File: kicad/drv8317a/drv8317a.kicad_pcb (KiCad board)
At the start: 2 copper layers, 15 parts, among them J1 Conn_01x08_Pin, J2 Conn_01x02_Pin, J3 Conn_01x03_Pin, J4 Conn_01x06_Pin, U1 DRV8317H

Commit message: 100% routed, review needed
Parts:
- NT1: moved to B.Cu
- moved J1 83.9 mm to (170.1, 110.4), turned to -90 degrees
- moved R1 68.8 mm to (163.3, 114.4), turned to -90 degrees
- moved J4 65.0 mm to (152.4, 126.7), turned to 180 degrees
- moved C4 8.45 mm to (164.7, 127.0)
- moved J2 8.19 mm to (178.8, 133.0), turned to 180 degrees
- moved C3 7.96 mm to (164.5, 128.8)
- moved C8 6.65 mm to (166.2, 124.3)
- moved NT1 6.04 mm to (168.8, 130.7)
- moved C9 1.75 mm to (163.3, 117.7), turned to 90 degrees
- moved C6 1.50 mm to (168.3, 126.1)
- moved C5 1.49 mm to (169.6, 114.3), turned to 0 degrees
- moved C7 1.30 mm to (169.8, 124.3)
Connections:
- J1 pad 1: /nSLEEP -> /INHA
- J1 pad 2: /INHA -> /INHB
- J1 pad 3: /INHB -> /INHC
- J1 pad 4: /INHC -> /INL
- J1 pad 5: /INL -> /GAIN
- J1 pad 6: /GAIN -> /SLEW
- J1 pad 7: /SLEW -> /MODE
- J1 pad 8: /MODE -> /nSLEEP
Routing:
- net GNDA: track 2.07 -> 30.6 mm, vias 0 -> 2
- net /INL: track 0.00 -> 24.9 mm, vias 0 -> 2
- net /nSLEEP: track 0.00 -> 22.4 mm, vias 0 -> 2
- net /nFAULT: track 0.00 -> 17.0 mm
- net /MODE: track 0.00 -> 15.2 mm
- net /SOA: track 0.00 -> 14.8 mm
- net /SLEW: track 0.00 -> 13.9 mm
- net /SOB: track 0.00 -> 13.9 mm
- net GNDPWR: track 7.90 -> 21.4 mm, vias 4 -> 11
- net /SOC: track 0.00 -> 13.4 mm
- net VDDA: track 0.00 -> 11.5 mm, vias 0 -> 2
- net /GAIN: track 0.00 -> 11.0 mm
- net +BATT: track 11.6 -> 21.5 mm, vias 2 -> 7
- net /INHA: track 0.00 -> 8.07 mm
- net /INHB: track 0.00 -> 7.43 mm
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- added copper zone on B.Cu, net +BATT
- added copper zone on B.Cu, net GNDA
- added copper zone on B.Cu, net GNDPWR
- added copper zone on F.Cu, net GNDPWR
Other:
- board outline added: 31.3 x 25.2 mm

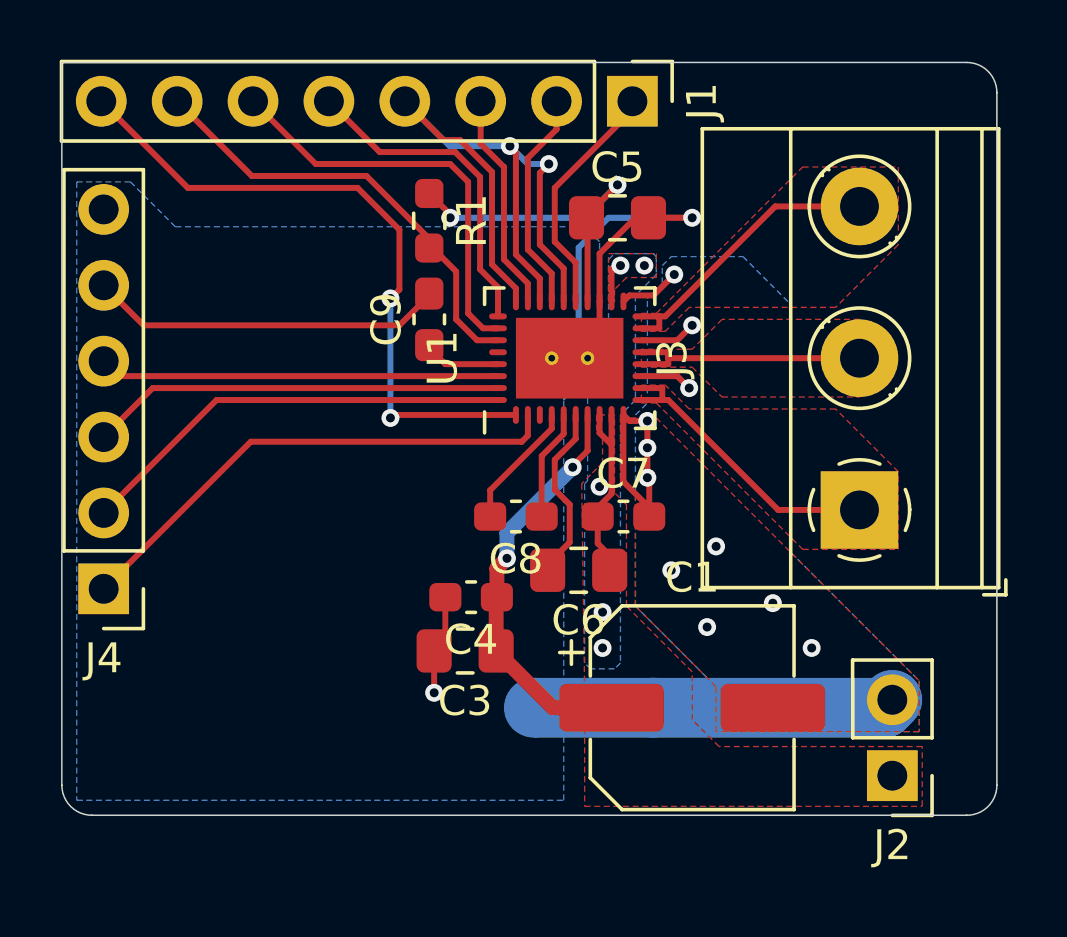
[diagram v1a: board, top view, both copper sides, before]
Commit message: config: use resistors instead of mcu signals
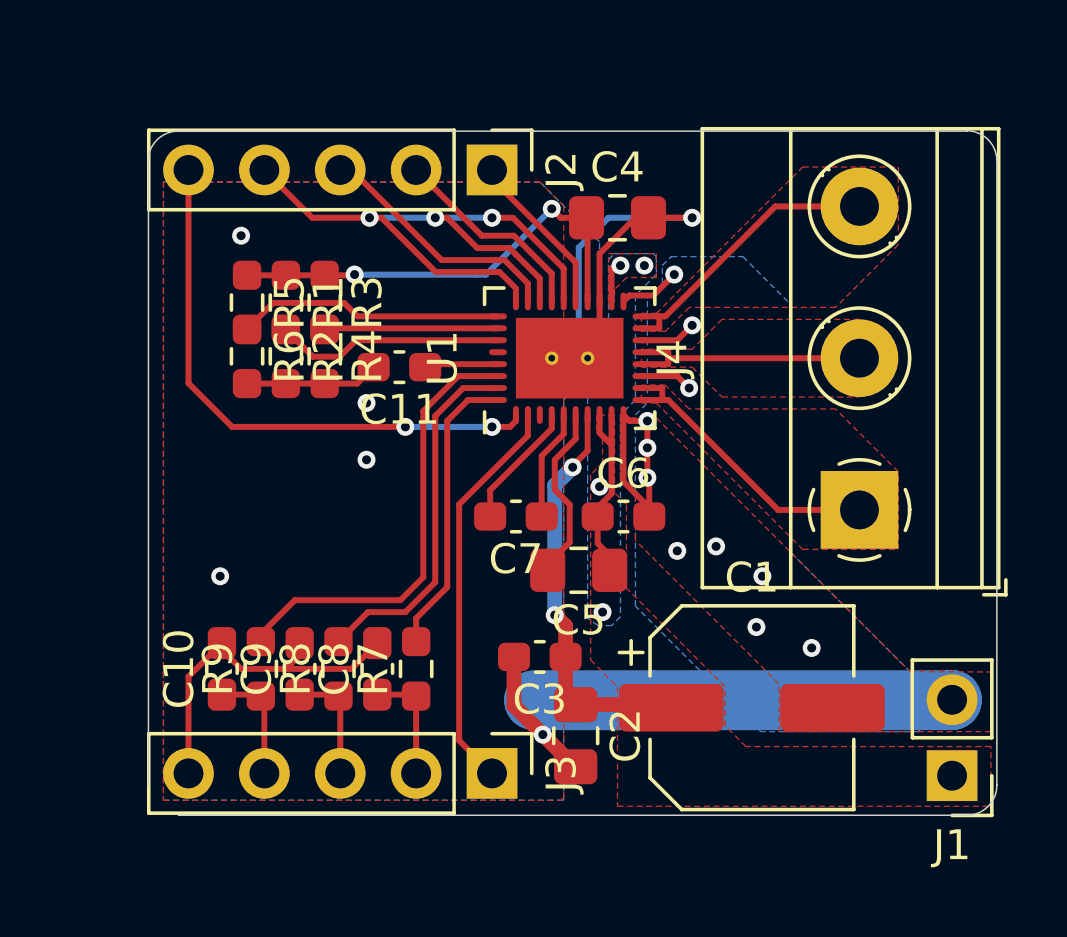
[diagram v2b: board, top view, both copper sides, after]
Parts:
- removed the J1 at (170.1, 110.4)
- removed the J4 at (152.4, 126.7)
- added C10: 22pF, Capacitor_SMD:C_0603_1608Metric_Pad1.08x0.95mm_HandSolder, F.Cu at (156.4, 129.4)
- added C8: 22pF, Capacitor_SMD:C_0603_1608Metric_Pad1.08x0.95mm_HandSolder, F.Cu at (161.6, 129.4)
- added C9: 22pF, Capacitor_SMD:C_0603_1608Metric_Pad1.08x0.95mm_HandSolder, F.Cu at (159.0, 129.4)
- added J2: Conn_01x05_Pin, Connector_PinHeader_2.54mm:PinHeader_1x05_P2.54mm_Vertical, F.Cu at (165.4, 112.7)
- added J3: Conn_01x05_Pin, Connector_PinHeader_2.54mm:PinHeader_1x05_P2.54mm_Vertical, F.Cu at (165.4, 132.9)
- added R2: NC, Resistor_SMD:R_0603_1608Metric_Pad0.98x0.95mm_HandSolder, F.Cu at (158.5, 118.9)
- added R3: NC, Resistor_SMD:R_0603_1608Metric_Pad0.98x0.95mm_HandSolder, F.Cu at (159.8, 117.1)
- added R4: NC, Resistor_SMD:R_0603_1608Metric_Pad0.98x0.95mm_HandSolder, F.Cu at (159.8, 118.9)
- added R5: NC, Resistor_SMD:R_0603_1608Metric_Pad0.98x0.95mm_HandSolder, F.Cu at (157.2, 117.1)
- added R6: NC, Resistor_SMD:R_0603_1608Metric_Pad0.98x0.95mm_HandSolder, F.Cu at (157.2, 118.9)
- added R7: 330R, Resistor_SMD:R_0603_1608Metric_Pad0.98x0.95mm_HandSolder, F.Cu at (162.9, 129.4)
- added R8: 330R, Resistor_SMD:R_0603_1608Metric_Pad0.98x0.95mm_HandSolder, F.Cu at (160.3, 129.4)
- added R9: 330R, Resistor_SMD:R_0603_1608Metric_Pad0.98x0.95mm_HandSolder, F.Cu at (157.7, 129.4)
- R1: value 10k -> NC
- moved R1 5.53 mm to (158.5, 117.1)
- moved C2 4.66 mm to (168.2, 131.6), turned to -90 degrees
- moved C3 3.05 mm to (167.0, 129.0)
- moved C1 2.00 mm to (174.1, 130.7)
- moved J1 2.00 mm to (180.8, 133.0)
- moved C11 1.89 mm to (162.3, 119.3), turned to 180 degrees
- moved NT1 0.25 mm to (168.8, 130.4)
- renumbered C9 to C11, C3 to C2, C4 to C3, C5 to C4, C6 to C5, C7 to C6, C8 to C7, J2 to J1, J3 to J4
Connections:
- net Net-(U1-CSA_REF) renamed /CSA
- U1 pad 34: /SOC -> Net-(U1-SOC)
- U1 pad 35: /SOB -> Net-(U1-SOB)
- U1 pad 36: /SOA -> Net-(U1-SOA)
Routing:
- net Net-(U1-SOC): track 0.00 -> 15.0 mm
- net Net-(U1-SOB): track 0.00 -> 12.4 mm
- net /SOA: track 14.8 -> 3.91 mm
- net /SOB: track 13.9 -> 3.93 mm
- net Net-(U1-SOA): track 0.00 -> 9.81 mm
- net /SOC: track 13.4 -> 3.96 mm
- net /SLEW: track 13.9 -> 5.81 mm
- net /MODE: track 15.2 -> 7.70 mm
- net GNDA: track 30.6 -> 36.2 mm, vias 2 -> 6
- net VDDA: track 11.5 -> 15.2 mm
- net /nFAULT: track 17.0 -> 13.4 mm
- net /nSLEEP: track 22.4 -> 19.0 mm
- net /INHA: track 8.07 -> 5.56 mm
- net /GAIN: track 11.0 -> 8.95 mm
- net GNDPWR: track 21.4 -> 23.3 mm
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- added copper zone on F.Cu, net GNDA
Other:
- board size 31.3 x 25.2 mm -> 28.4 x 22.9 mm

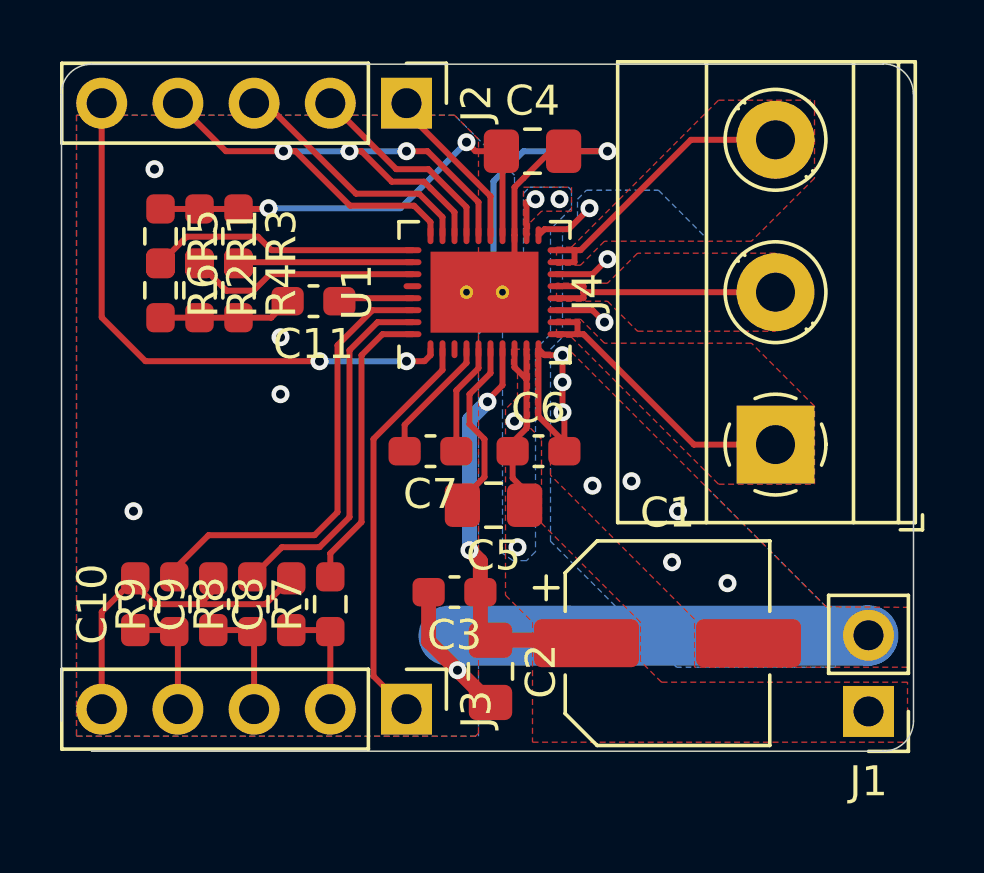
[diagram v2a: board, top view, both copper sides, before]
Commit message: pcb DRV8317a all done
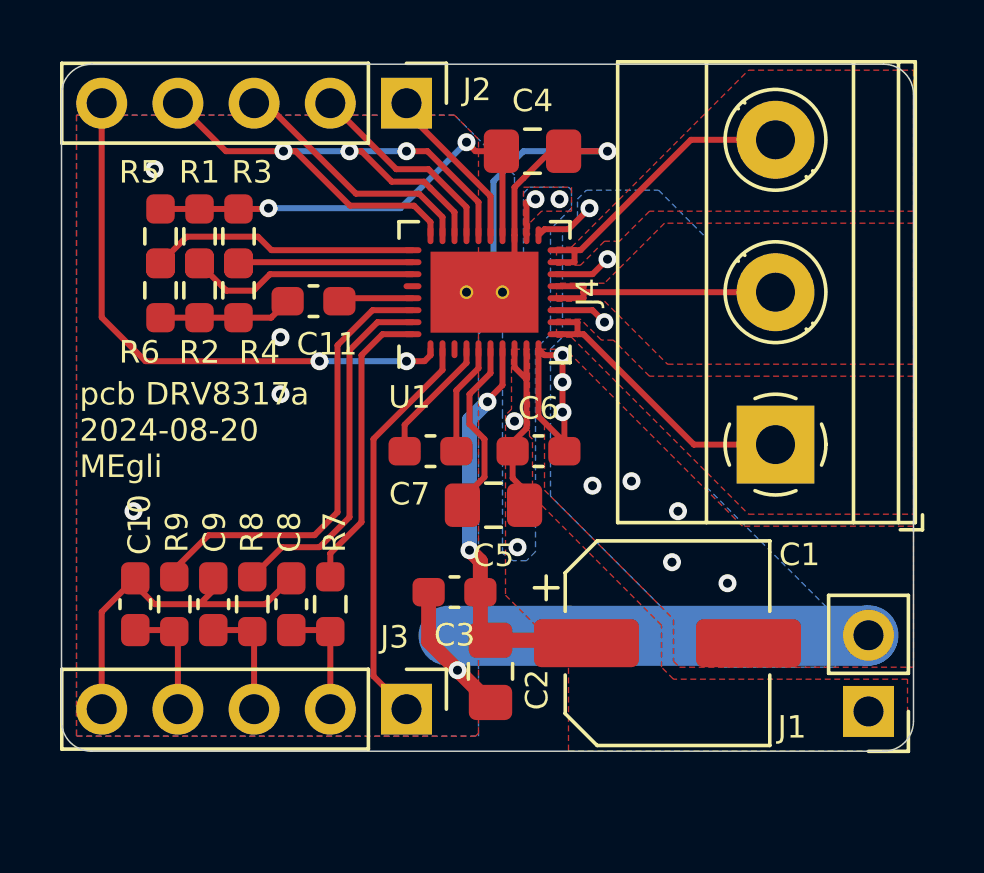
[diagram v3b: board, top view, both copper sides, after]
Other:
- outline, holes or cut-outs redrawn
- board text added: "pcb DRV8317a 2024-08-20 MEgli"

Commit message: ready to order pcbs
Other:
- board text added: "GND"
- board text added: "GNDA"
- board text added: "INHA"
- board text added: "INHB"
- board text added: "INHC"
- board text added: "INL"
- board text added: "SOA"
- board text added: "SOB"
- board text added: "SOC"
- board text added: "nFAULT"
- board text added: "nSLEEP"
